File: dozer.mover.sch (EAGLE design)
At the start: 10 parts, among them IC1 PIC18F4550_40, U1 L298, U2 L298

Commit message: Renamed parts at Mhisani's behest
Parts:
- renumbered U$1 to J1
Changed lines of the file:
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@@
 </classes>
 <parts>
-<part name="U$1" library="RaspberryPi" deviceset="RASPBERRY-PI" device=""/>
+<part name="J1" library="RaspberryPi" deviceset="RASPBERRY-PI" device="" value=""/>
 <part name="IC1" library="microchip" deviceset="PIC18F4*_40" device="" technology="550"/>
 <part name="Y1" library="SparkFun-FreqCtrl" deviceset="RESONATOR" device="PTH"/>
@@
 </plain>
 <instances>
-<instance part="U$1" gate="G$1" x="38.1" y="22.86"/>
+<instance part="J1" gate="G$1" x="38.1" y="22.86"/>
 <instance part="IC1" gate="G$1" x="187.96" y="53.34"/>
 <instance part="Y1" gate="G$1" x="185.42" y="114.3" rot="R90"/>
@@
 </segment>
 <segment>
-<pinref part="U$1" gate="G$1" pin="6-GND"/>
+<pinref part="J1" gate="G$1" pin="6-GND"/>
 <wire x1="66.04" y1="63.5" x2="81.28" y2="63.5" width="0.1524" layer="91"/>
 <wire x1="81.28" y1="63.5" x2="83.82" y2="66.04" width="0.1524" layer="91"/>
@@
 <net name="5VDC" class="0">
 <segment>
-<pinref part="U$1" gate="G$1" pin="2-+5V"/>
+<pinref part="J1" gate="G$1" pin="2-+5V"/>
 <wire x1="66.04" y1="73.66" x2="81.28" y2="73.66" width="0.1524" layer="91"/>
 <wire x1="81.28" y1="73.66" x2="83.82" y2="76.2" width="0.1524" layer="91"/>
@@
 <net name="UARTTX" class="0">
 <segment>
-<pinref part="U$1" gate="G$1" pin="8-TX"/>
+<pinref part="J1" gate="G$1" pin="8-TX"/>
 <wire x1="66.04" y1="58.42" x2="81.28" y2="58.42" width="0.1524" layer="91"/>
 <wire x1="81.28" y1="58.42" x2="83.82" y2="60.96" width="0.1524" layer="91"/>
@@
 <net name="UARTRX" class="0">
 <segment>
-<pinref part="U$1" gate="G$1" pin="10-RX"/>
+<pinref part="J1" gate="G$1" pin="10-RX"/>
 <wire x1="66.04" y1="53.34" x2="81.28" y2="53.34" width="0.1524" layer="91"/>
 <wire x1="81.28" y1="53.34" x2="83.82" y2="55.88" width="0.1524" layer="91"/>

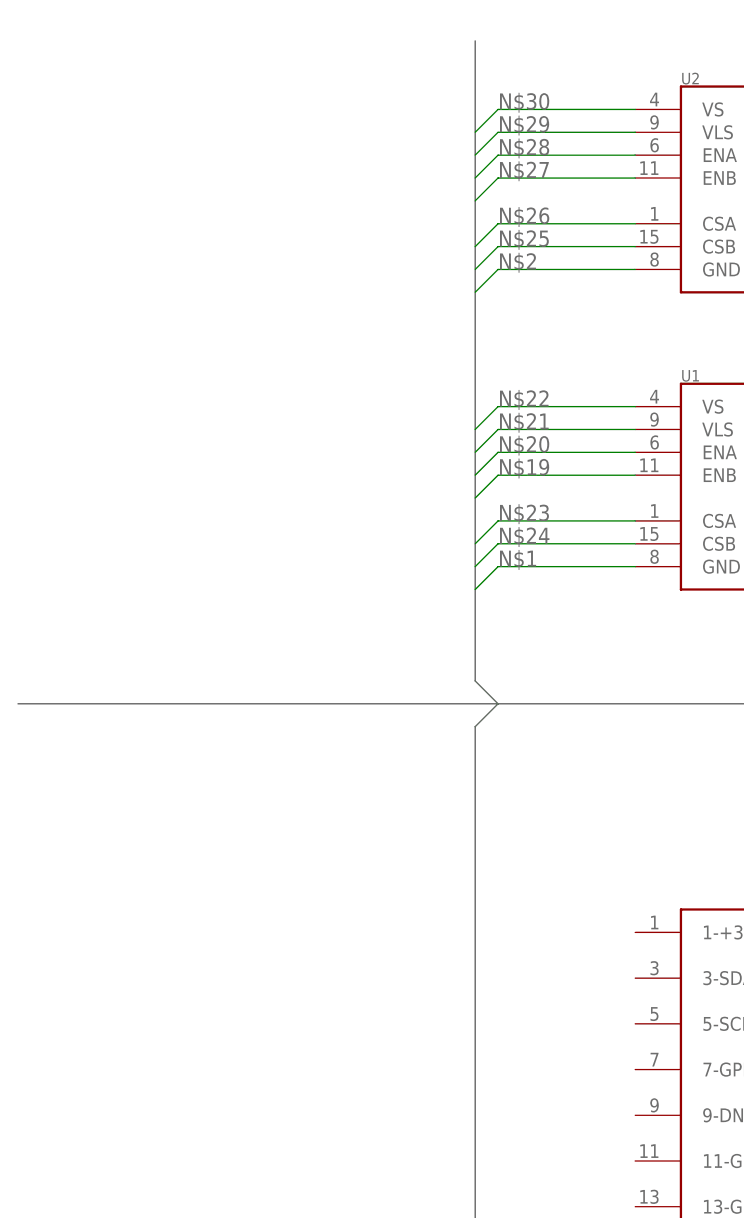
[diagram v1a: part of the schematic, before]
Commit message: Added beefy 5v vreg for both internal supply and powering the Raspberry Pi
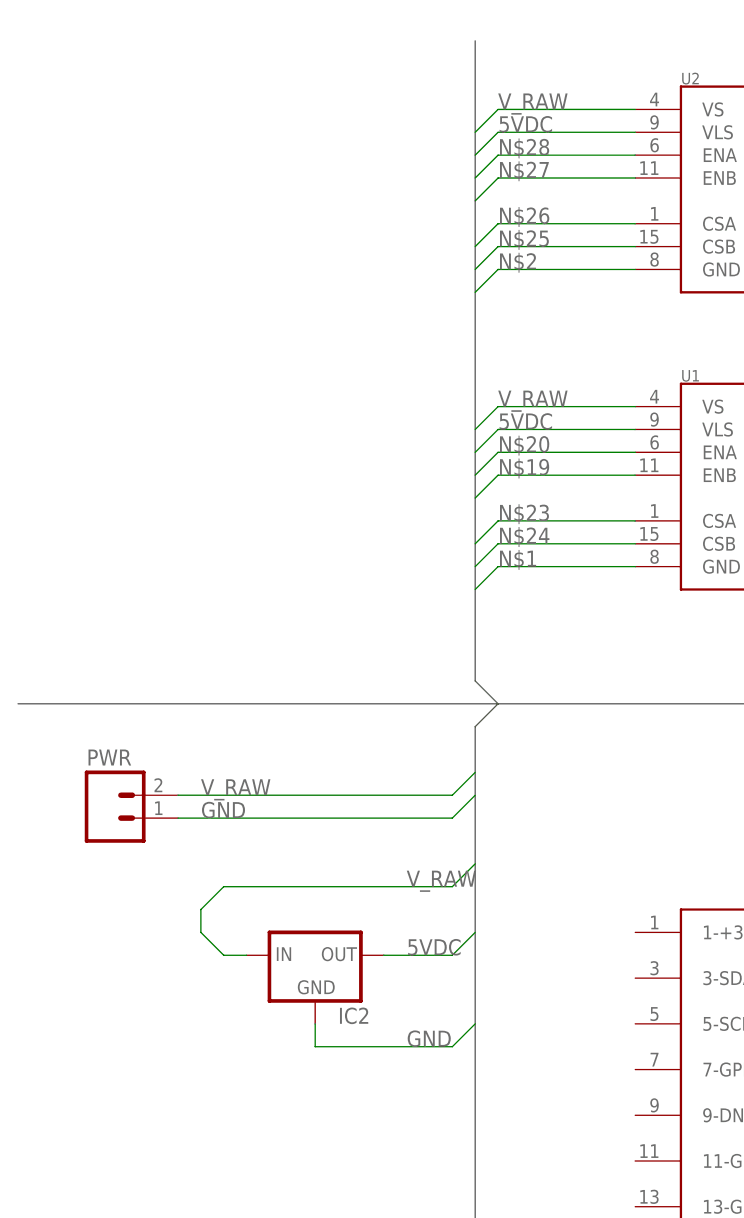
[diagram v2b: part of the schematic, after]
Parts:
- added IC2: (no value), SparkFun-PowerIC:V_REG_78XXSINK
- added PWR: (no value), SparkFun-Connectors:M02JST-PTH-2
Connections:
- removed net N$21: U1.VLS
- removed net N$22: U1.VS
- removed net N$29: U2.VLS
- removed net N$30: U2.VS
- new net V_RAW: IC2.IN, PWR.2, U1.VS, U2.VS
- net 5VDC: now also IC2.OUT, U1.VLS, U2.VLS
- net GND: now also IC2.GND, PWR.1

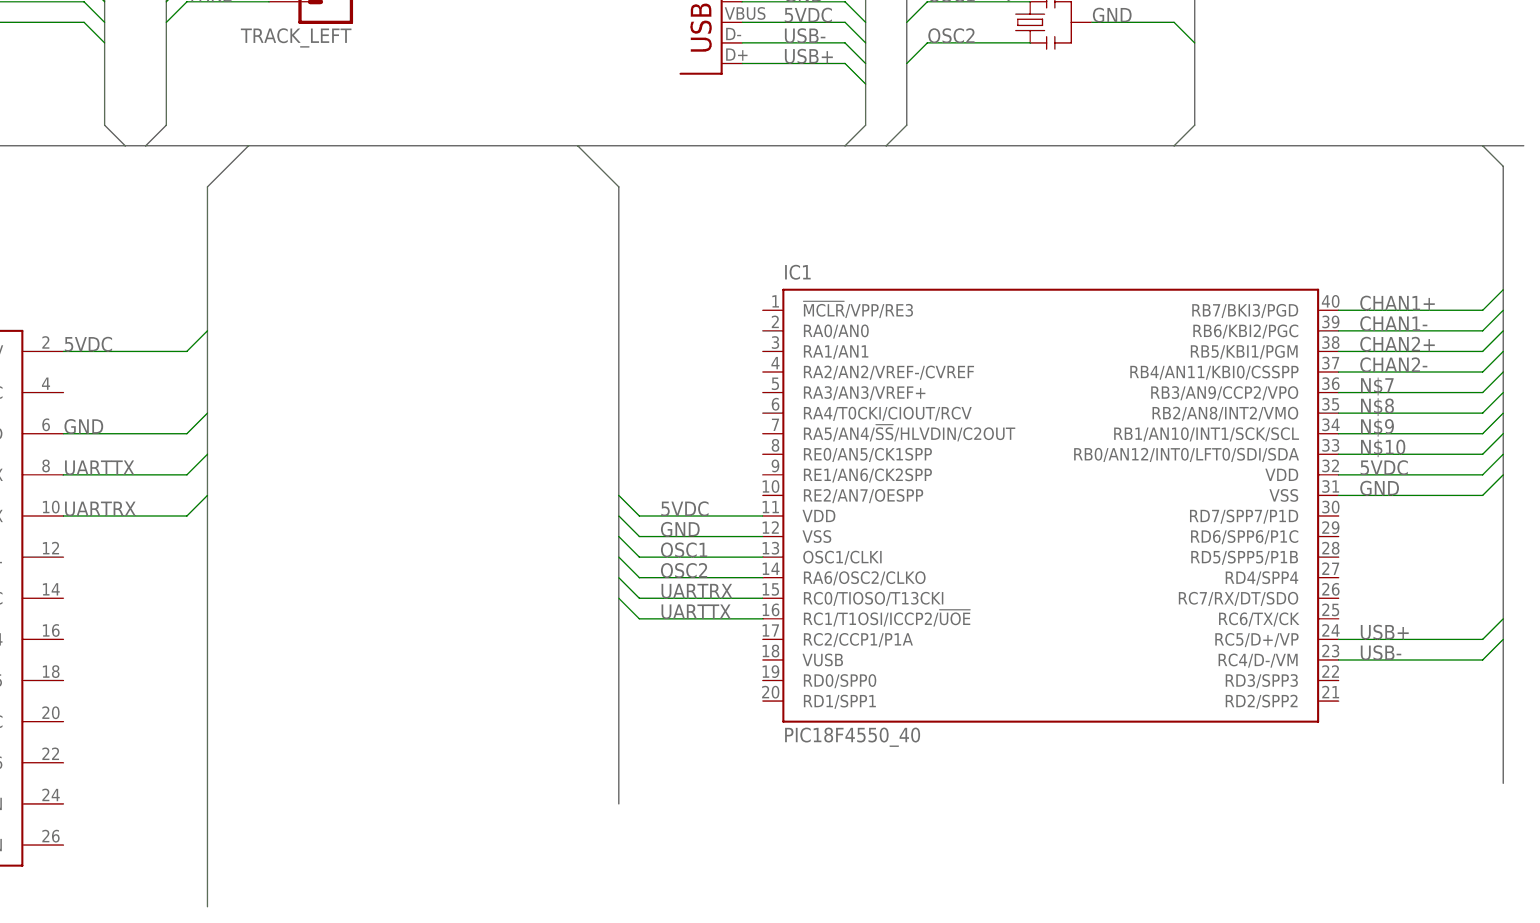
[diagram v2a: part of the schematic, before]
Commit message: Migrate motor controls further down interface B, frees up GPIO to use for ICSP without having to add loads of resistors. Also added reset circuit required to make PIC run, but not actually a reset switch.
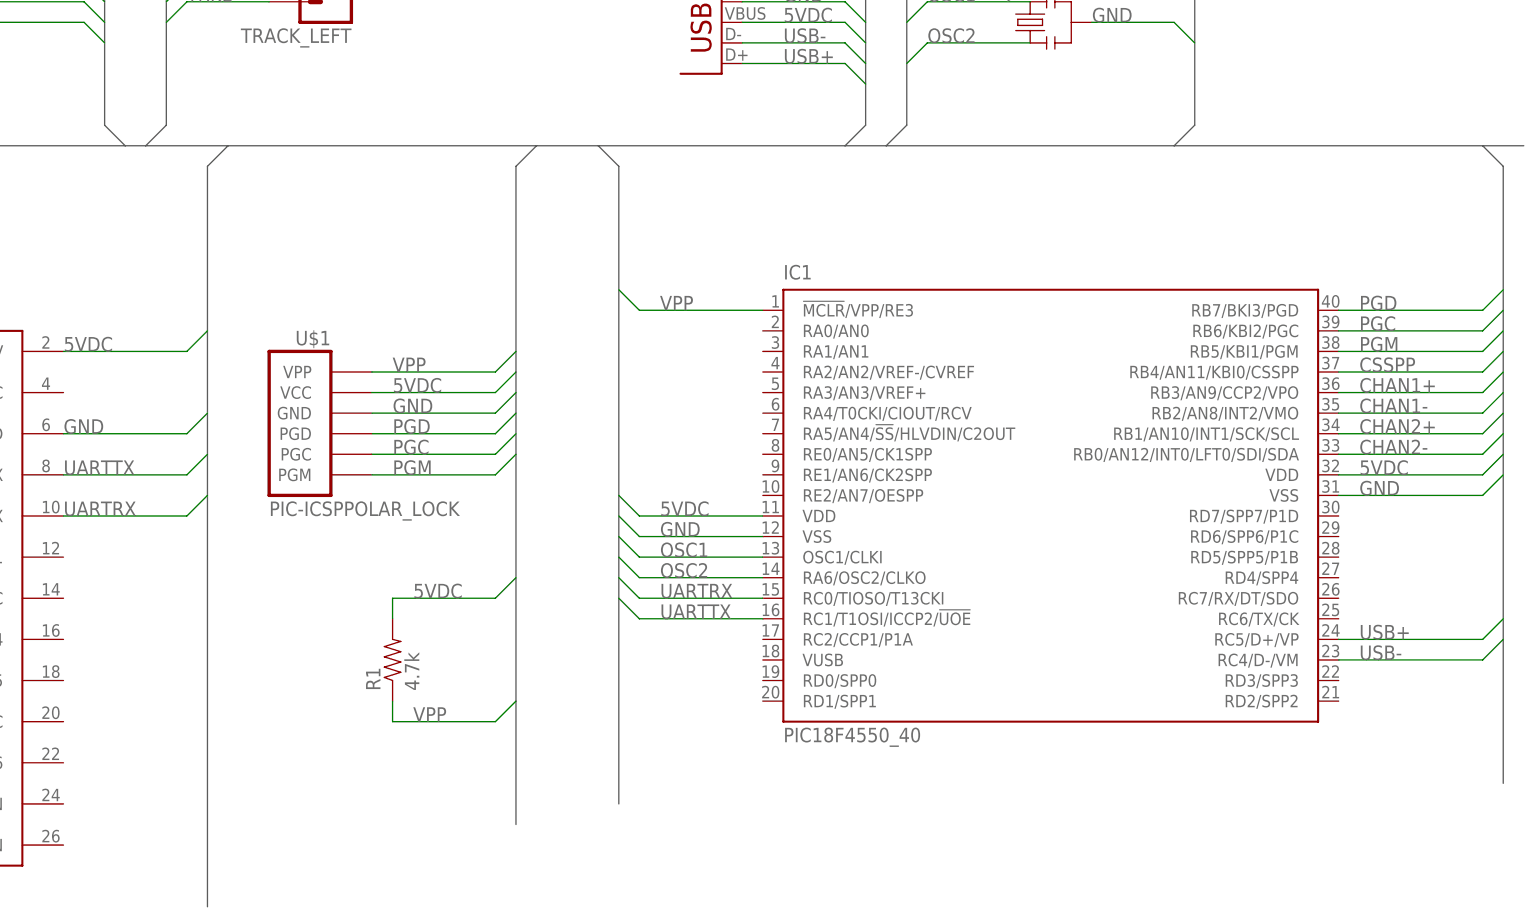
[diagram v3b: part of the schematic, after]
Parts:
- added R1: 4.7k, SparkFun-Resistors:RESISTORPTH-1/4W
- added U$1: PIC-ICSPPOLAR_LOCK, SparkFun-Connectors:PIC-ICSPPOLAR_LOCK
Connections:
- removed net N$10: IC1.RB0/AN12/INT0/LFT0/SDI/SDA
- removed net N$7: IC1.RB3/AN9/CCP2/VPO
- removed net N$8: IC1.RB2/AN8/INT2/VMO
- removed net N$9: IC1.RB1/AN10/INT1/SCK/SCL
- new net CSSPP: IC1.RB4/AN11/KBI0/CSSPP
- new net PGC: IC1.RB6/KBI2/PGC, U$1.PGC
- new net PGD: IC1.RB7/BKI3/PGD, U$1.PGD
- new net PGM: IC1.RB5/KBI1/PGM, U$1.PGM
- new net VPP: IC1.!MCLR!/VPP/RE3, R1.1, U$1.VPP
- net 5VDC: now also R1.2, U$1.VCC
- net CHAN1+: now also IC1.RB3/AN9/CCP2/VPO; no longer IC1.RB7/BKI3/PGD
- net CHAN1-: now also IC1.RB2/AN8/INT2/VMO; no longer IC1.RB6/KBI2/PGC
- net CHAN2+: now also IC1.RB1/AN10/INT1/SCK/SCL; no longer IC1.RB5/KBI1/PGM
- net CHAN2-: now also IC1.RB0/AN12/INT0/LFT0/SDI/SDA; no longer IC1.RB4/AN11/KBI0/CSSPP
- net GND: now also U$1.GND
